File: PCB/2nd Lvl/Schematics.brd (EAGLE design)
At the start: 62 x 62 mm, 15 parts, among them U14 XBEE-1B1, U15 IT530, U16 SDTR1130, U17 ANTENNA2SMD6

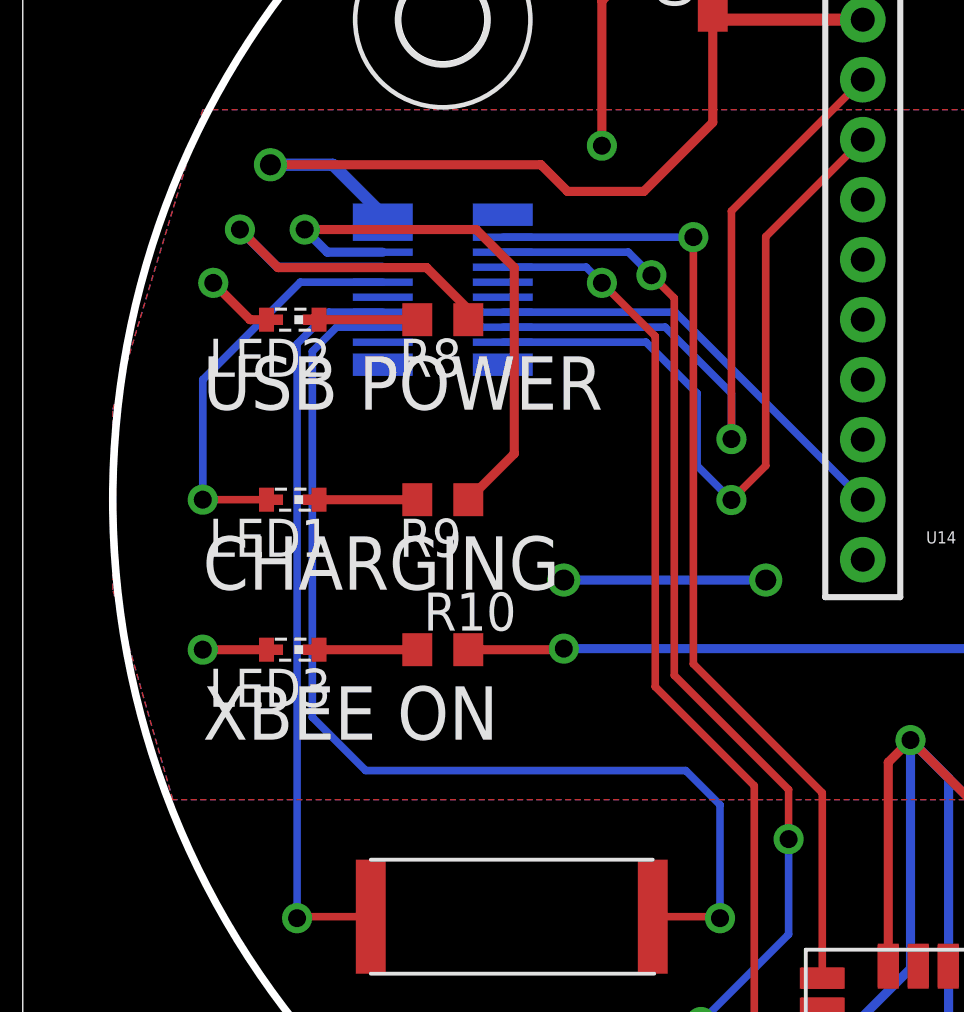
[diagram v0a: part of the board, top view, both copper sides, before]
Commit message: Added GPS_FIX Led to 2nd lvl
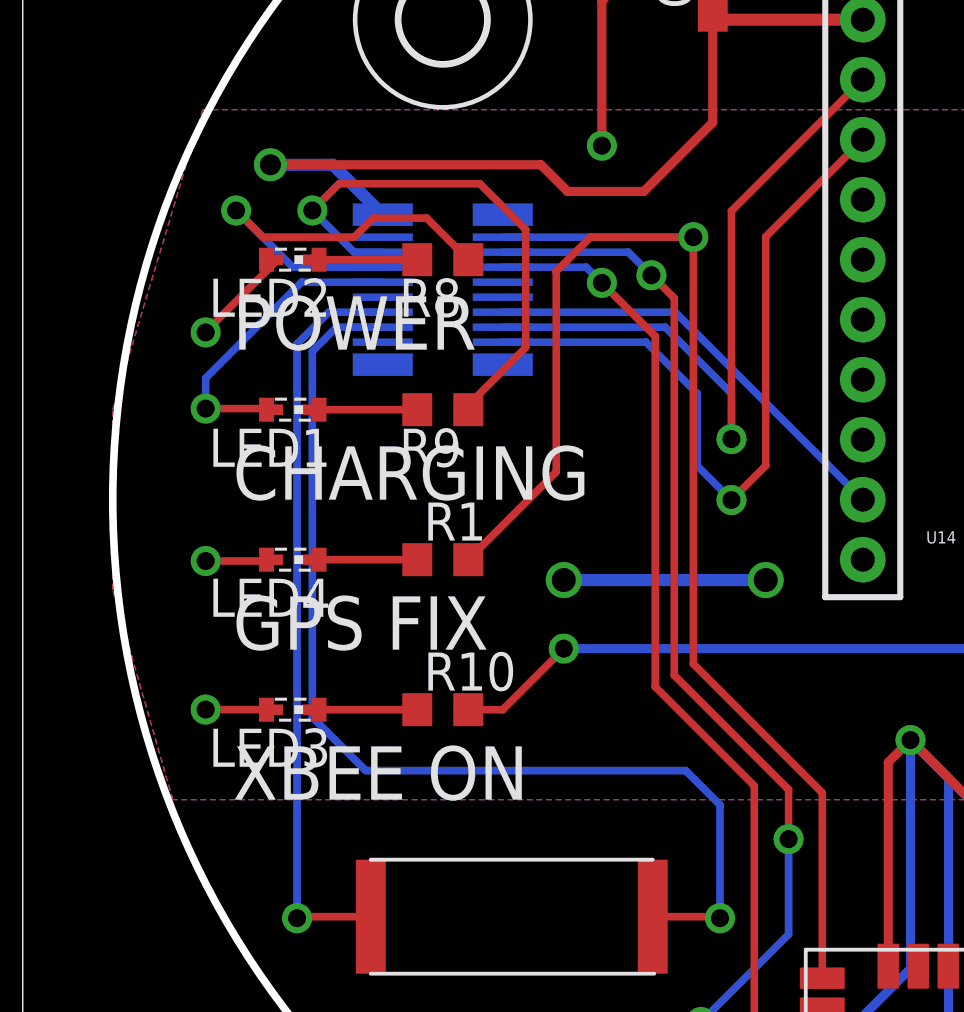
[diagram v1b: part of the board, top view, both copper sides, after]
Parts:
- added LED4: (no value), led:SMARTLED-TTW
- added R1: 1.5k, rcl:R0603
- moved LED1 3.00 mm to (9.00, 34.0)
- moved R9 3.00 mm to (14.0, 34.0)
- moved LED2 2.00 mm to (9.00, 39.0)
- moved LED3 2.00 mm to (9.00, 24.0)
- moved R10 2.00 mm to (14.0, 24.0)
- moved R8 2.00 mm to (14.0, 39.0)
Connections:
- new net N$1: LED4.A@1, R1.1
- net GND: now also LED4.C@1
- net GPS_FIX: now also R1.2
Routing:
- net GPS_FIX: track 32.8 -> 48.7 mm
- net N$1: track 0.00 -> 3.65 mm
- net LED1: track 13.8 -> 10.7 mm
- net GND: track 113.0 -> 116.1 mm, vias 8 -> 9
- net CHRG_VCC: track 18.8 -> 17.8 mm
- net N$4: track 38.0 -> 38.9 mm
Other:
- board text added: "GPS FIX"
- board text added: "POWER"
- board text removed: "USB POWER"

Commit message: Updated schematic values
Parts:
- R11: value 1.5k -> 50
- renumbered R1 to R11
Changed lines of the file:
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@@
 <?xml version="1.0" encoding="utf-8"?>
 <!DOCTYPE eagle SYSTEM "eagle.dtd">
-<eagle version="6.2">
+<eagle version="6.0">
 <drawing>
 <settings>
@@
 <element name="U$5" library="holes" package="2,8" value="" x="45" y="12"/>
 <element name="LED4" library="led" package="SMARTLED-TTW" value="" x="9" y="29" rot="R90"/>
-<element name="R1" library="rcl" package="R0603" value="1.5k" x="14" y="29"/>
+<element name="R11" library="rcl" package="R0603" value="50" x="14" y="29"/>
 </elements>
 <signals>
@@
 <wire x1="22.352" y1="25.527" x2="26.65" y2="21.229" width="0.254" layer="1"/>
 <wire x1="26.65" y1="21.229" x2="26.65" y2="15.05" width="0.254" layer="1"/>
-<contactref element="R1" pad="2"/>
+<contactref element="R11" pad="2"/>
 <wire x1="14.85" y1="29" x2="17.78" y2="31.93" width="0.254" layer="1"/>
 <wire x1="17.78" y1="31.93" x2="17.78" y2="38.608" width="0.254" layer="1"/>
@@
 </signal>
 <signal name="N$1">
-<contactref element="R1" pad="1"/>
+<contactref element="R11" pad="1"/>
 <contactref element="LED4" pad="A@1"/>
 <wire x1="9.5" y1="29" x2="13.15" y2="29" width="0.254" layer="1"/>
